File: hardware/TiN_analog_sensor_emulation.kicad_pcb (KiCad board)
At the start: 2 copper layers, 100 x 100 mm, 176 parts, among them J1 ADc, J2 Conn_01x04_Male, J3 Micro_SD_Card, J4 BOOT0, J5 Conn_01x03_Male, J6 display, J7 Barrel_Jack, J8 Conn_02x08_Odd_Even, SW2 SW_right, SW3 SW_middle2, SW4 SW_top, SW5 SW_middle, SW6 SW_bot, SW7 SW_Left, U1 STM32F042C6Tx, U10 MCP42010, U11 ADA4898-3, U12 ADA4898-3, U13 MCP42010, U14 MCP42010, U15 MCP42050, U16 MCP42050, U17 MCP42050, U18 LT1529CQ#PBF, U19 LT1528CQ, U2 ADA4898-3, U3 ADA4898-3, U4 MCP42010, U5 ADA4898-3, U6 ADA4898-3, U7 MCP42010, U8 ADA4898-3, U9 ADA4898-3, Y1 Crystal_GND24

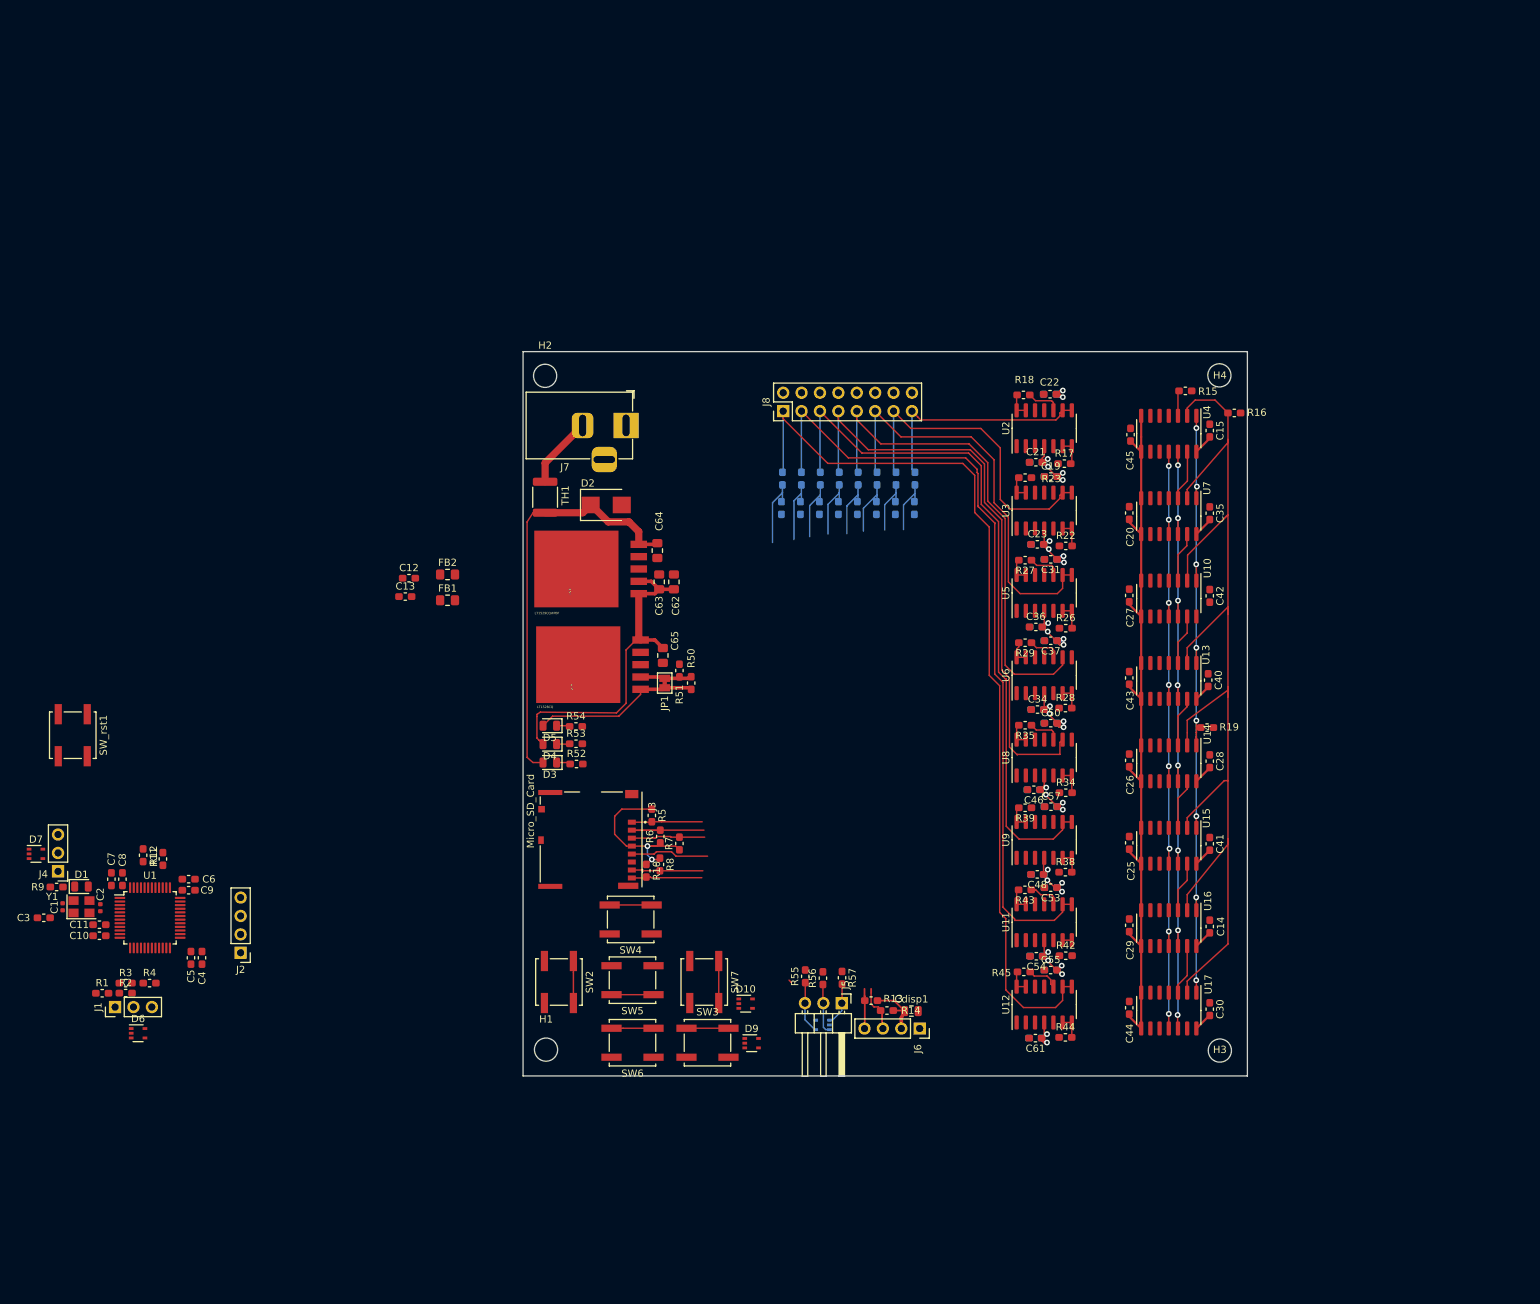
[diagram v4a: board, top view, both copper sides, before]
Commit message: layout gotów, do wyeliminowania błedy DRC
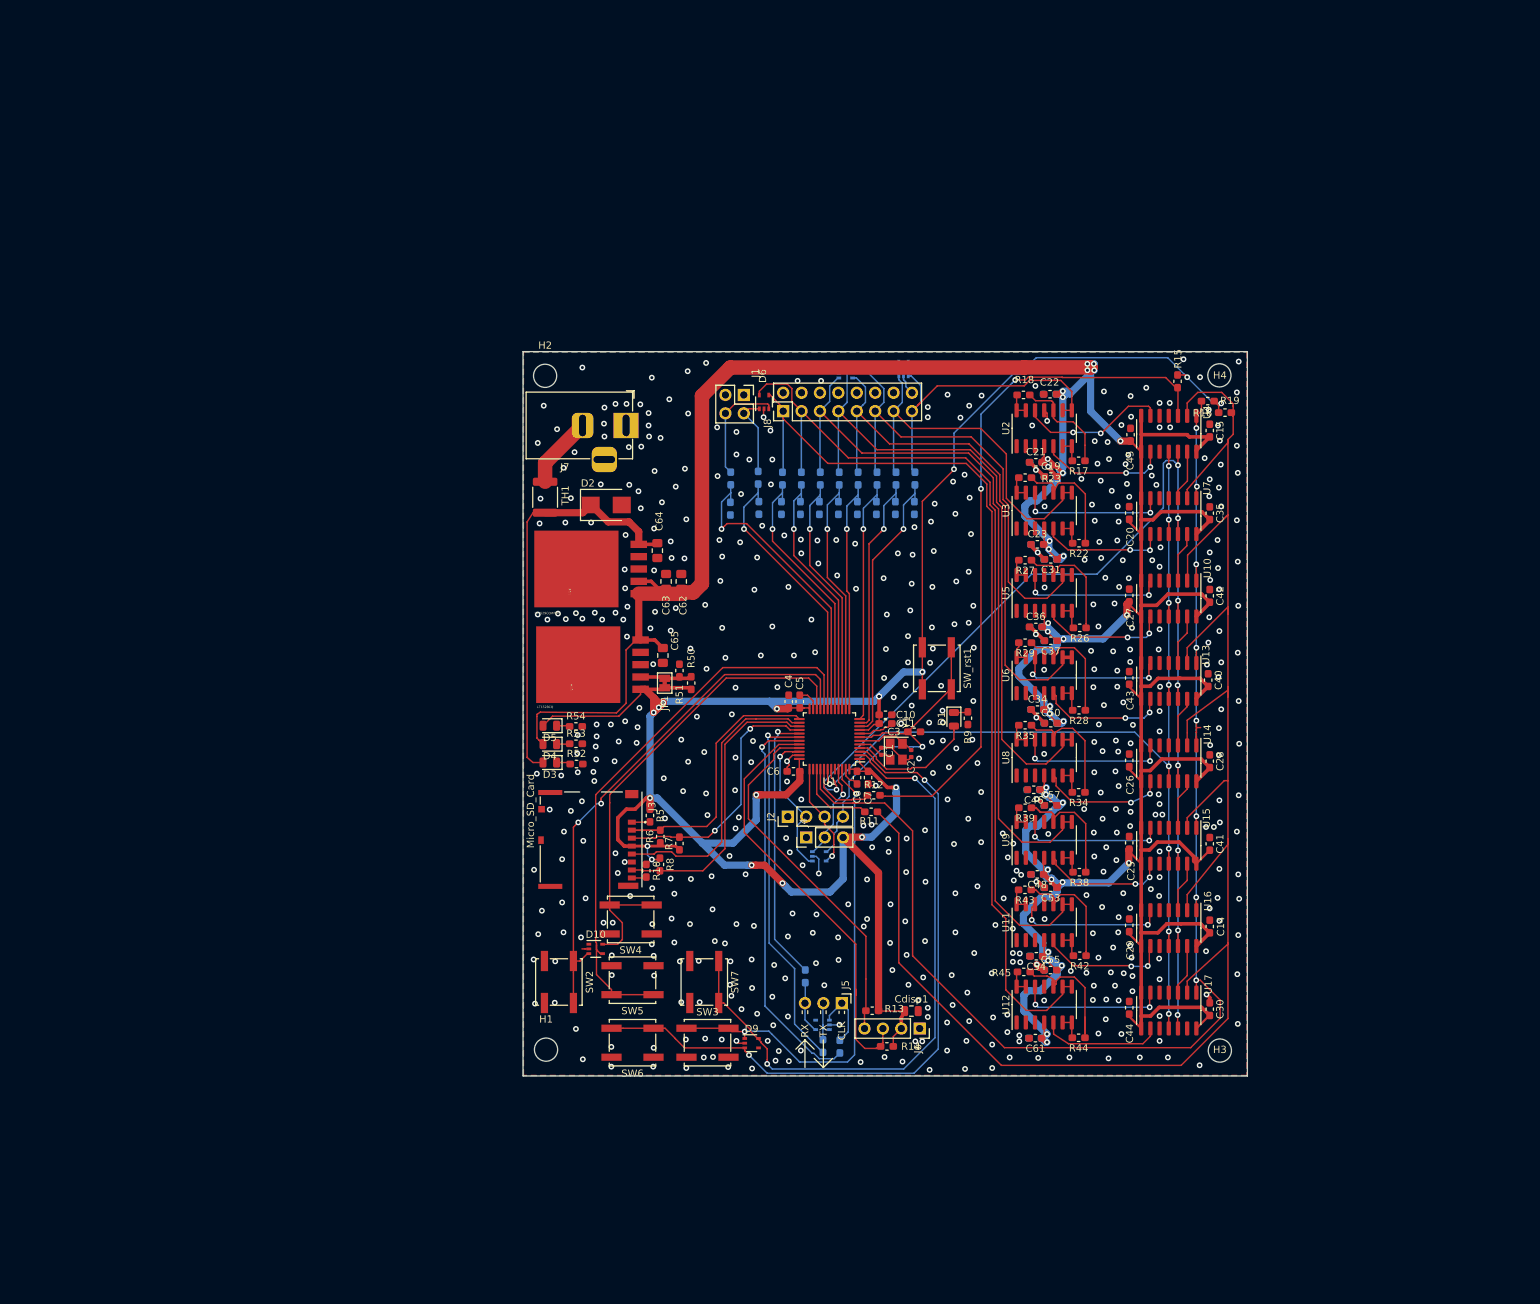
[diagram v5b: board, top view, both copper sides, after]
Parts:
- removed C12: 1u, Capacitor_SMD:C_0603_1608Metric_Pad1.05x0.95mm_HandSolder
- removed C13: 10n, Capacitor_SMD:C_0603_1608Metric_Pad1.05x0.95mm_HandSolder
- removed C9: 100n, Capacitor_SMD:C_0603_1608Metric_Pad1.05x0.95mm_HandSolder
- removed FB1, FB2: Ferrite_Bead_Small, Inductor_SMD:L_0805_2012Metric_Pad1.15x1.40mm_HandSolder
- added D11: PESD5V0L4UG, Package_TO_SOT_SMD:SOT-353_SC-70-5, B.Cu at (147.5, 52.4)
- added D12: PESD5V0L4UG, Package_TO_SOT_SMD:SOT-353_SC-70-5, B.Cu at (139.5, 53.0)
- D7, R1, R2, R3, R4, R55, R56, R57: moved to B.Cu
- J1: value ADc -> Conn_02x02_Odd_Even; footprint Connector_PinHeader_2.54mm:PinHeader_1x03_P2.54mm_Vertical -> Connector_PinHeader_2.54mm:PinHeader_2x02_P2.54mm_Vertical
- moved R9 127.9 mm to (156.4, 100.6), turned to 270 degrees
- moved C3 122.9 mm to (149.0, 102.5)
- moved D6 122.7 mm to (128.3, 56.9), turned to 90 degrees
- moved D1 122.6 mm to (154.5, 100.8), turned to 270 degrees
- moved J1 121.1 mm to (125.5, 56.0), turned to 270 degrees
- moved SW_rst1 119.6 mm to (152.1, 93.7)
- moved C1 115.0 mm to (144.4, 105.2), turned to 90 degrees
- moved Y1 114.5 mm to (146.5, 105.2), turned to 270 degrees
- moved C2 114.0 mm to (148.6, 105.5), turned to 90 degrees
- moved C10 112.7 mm to (145.0, 100.1), turned to 0 degrees
- moved R1 112.2 mm to (123.7, 67.5), turned to 270 degrees
- moved C11 112.0 mm to (145.0, 101.3), turned to 0 degrees
- moved R3 111.8 mm to (127.5, 67.4), turned to 270 degrees
- moved D7 108.1 mm to (135.9, 119.7)
- moved R2 107.0 mm to (123.6, 71.7), turned to 270 degrees
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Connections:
- C10 pad 2: GNDA -> GND
- C11 pad 2: GNDA -> GND
- C16 pad 2: GNDA -> GND
- C17 pad 1: GNDA -> GND
- C18 pad 2: GNDA -> GND
- C19 pad 1: GNDA -> GND
- C21 pad 1: GNDA -> GND
- C22 pad 2: GNDA -> GND
- C23 pad 1: GNDA -> GND
- C24 pad 2: GNDA -> GND
- C31 pad 2: GNDA -> GND
- C32 pad 1: GNDA -> GND
- C33 pad 2: GNDA -> GND
- C34 pad 1: GNDA -> GND
- C36 pad 1: GNDA -> GND
- C37 pad 2: GNDA -> GND
- C38 pad 1: GNDA -> GND
- C39 pad 2: GNDA -> GND
- C4 pad 2: +3V3 -> +3.3VA
- C46 pad 2: GNDA -> GND
- C47 pad 1: GNDA -> GND
- C48 pad 2: GNDA -> GND
- C49 pad 1: GNDA -> GND
- C5 pad 2: +3V3 -> +3.3VA
- C50 pad 1: GNDA -> GND
- C51 pad 2: GNDA -> GND
- C52 pad 1: GNDA -> GND
- C53 pad 2: GNDA -> GND
- C54 pad 2: GNDA -> GND
- C55 pad 1: GNDA -> GND
- C56 pad 2: GNDA -> GND
- C57 pad 1: GNDA -> GND
- C58 pad 1: GNDA -> GND
- C59 pad 2: GNDA -> GND
- C6 pad 1: +3V3 -> +3.3VA
- C60 pad 1: GNDA -> GND
- C61 pad 2: GNDA -> GND
- C7 pad 1: +3V3 -> +3.3VA
- C8 pad 2: +3V3 -> +3.3VA
- Cdisp1 pad 1: +3V3 -> +3.3VA
- D10 pad 1: (no net) -> Net-(D10-Pad1)
- D10 pad 3: (no net) -> /MCU/sw_left
- D10 pad 5: (no net) -> /MCU/sw_top
- D6 pad 4: (no net) -> /digital_pot/pot8
- D6 pad 5: (no net) -> /digital_pot/pot7
- D7 pad 5: (no net) -> /MCU/SWCLK
- D9 pad 1: /MCU/sw_right -> /MCU/sw_mid2
- D9 pad 4: /MCU/sw_left -> (no net)
- D9 pad 5: (no net) -> /MCU/sw_right
- J1 pad 1: Net-(D6-Pad1) -> GND
- J1 pad 2: Net-(D6-Pad3) -> Net-(D6-Pad1)
- J3 pad 4: +3V3 -> +3.3VA
- J4 pad 3: +3V3 -> +3.3VA
- J6 pad 2: +3V3 -> +3.3VA
- J8 pad 10: GNDA -> GND
- J8 pad 12: GNDA -> GND
- J8 pad 14: GNDA -> GND
- J8 pad 16: GNDA -> GND
- J8 pad 2: GNDA -> GND
- J8 pad 4: GNDA -> GND
- J8 pad 6: GNDA -> GND
- J8 pad 8: GNDA -> GND
- R10 pad 1: +3V3 -> +3.3VA
- R13 pad 1: +3V3 -> +3.3VA
- R14 pad 1: +3V3 -> +3.3VA
- R15 pad 1: +3V3 -> +3.3VA
- R16 pad 1: +3V3 -> +3.3VA
- R19 pad 1: +3V3 -> +3.3VA
- R5 pad 1: +3V3 -> +3.3VA
- R6 pad 1: +3V3 -> +3.3VA
- R7 pad 1: +3V3 -> +3.3VA
- R8 pad 1: +3V3 -> +3.3VA
- SW_rst1 pad 1: +3V3 -> +3.3VA
- U1 pad 1: +3V3 -> +3.3VA
- U1 pad 24: +3V3 -> +3.3VA
- U1 pad 36: +3V3 -> +3.3VA
- U1 pad 48: +3V3 -> +3.3VA
- U1 pad 8: GNDA -> GND
- U10 pad 10: GNDA -> GND
- U10 pad 5: GNDA -> GND
- U11 pad 1: GNDA -> GND
- U11 pad 11: GNDA -> GND
- U11 pad 2: GNDA -> GND
- U11 pad 3: GNDA -> GND
- U12 pad 1: GNDA -> GND
- U12 pad 11: GNDA -> GND
- U12 pad 2: GNDA -> GND
- U12 pad 3: GNDA -> GND
- U13 pad 10: GNDA -> GND
- U13 pad 5: GNDA -> GND
- U14 pad 10: GNDA -> GND
- U14 pad 5: GNDA -> GND
- U15 pad 10: GNDA -> GND
- U15 pad 5: GNDA -> GND
- U16 pad 10: GNDA -> GND
- U16 pad 5: GNDA -> GND
- U17 pad 10: GNDA -> GND
- U17 pad 5: GNDA -> GND
- U2 pad 1: GNDA -> GND
- U2 pad 11: GNDA -> GND
- U2 pad 2: GNDA -> GND
- U2 pad 3: GNDA -> GND
- U3 pad 1: GNDA -> GND
- U3 pad 11: GNDA -> GND
- U3 pad 2: GNDA -> GND
- U3 pad 3: GNDA -> GND
- U4 pad 10: GNDA -> GND
- U4 pad 5: GNDA -> GND
- U5 pad 1: GNDA -> GND
- U5 pad 11: GNDA -> GND
- U5 pad 2: GNDA -> GND
- U5 pad 3: GNDA -> GND
- U6 pad 1: GNDA -> GND
- U6 pad 11: GNDA -> GND
- U6 pad 2: GNDA -> GND
- U6 pad 3: GNDA -> GND
- U7 pad 10: GNDA -> GND
- U7 pad 5: GNDA -> GND
- U8 pad 1: GNDA -> GND
- U8 pad 11: GNDA -> GND
- U8 pad 2: GNDA -> GND
- U8 pad 3: GNDA -> GND
- U9 pad 1: GNDA -> GND
- U9 pad 11: GNDA -> GND
- U9 pad 2: GNDA -> GND
- U9 pad 3: GNDA -> GND
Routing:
- net +5V: track 264.1 -> 588.5 mm
- net +3.3VA: track 23.1 -> 325.5 mm, vias 0 -> 18
- net /digital_pot/CS: track 94.6 -> 188.8 mm
- net /MCU/sw_bot: track 5.80 -> 98.9 mm, vias 0 -> 2
- net /MCU/POTMOSI: track 3.50 -> 96.3 mm, vias 0 -> 2
- net /MCU/POTSCK: track 157.6 -> 247.8 mm
- net /MCU/sw_right: track 5.80 -> 88.7 mm, vias 0 -> 2
- net /MCU/POTSHDN: track 92.2 -> 169.0 mm, vias 8 -> 9
- net /MCU/sw_mid1: track 5.80 -> 79.9 mm
- net /MCU/sw_left: track 5.80 -> 74.4 mm, vias 0 -> 2
- net /MCU/sw_top: track 5.80 -> 68.5 mm
- net /MCU/sw_mid2: track 5.80 -> 67.2 mm, vias 0 -> 2
- net /MCU/USART_CK: track 0.00 -> 55.1 mm, vias 0 -> 1
- net /MCU/POTRST: track 91.7 -> 145.6 mm, vias 8 -> 9
- net /MCU/I2C_SCL: track 6.52 -> 59.5 mm
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- added copper zone on B.Cu, net GND
- added copper zone on F.Cu, net GND

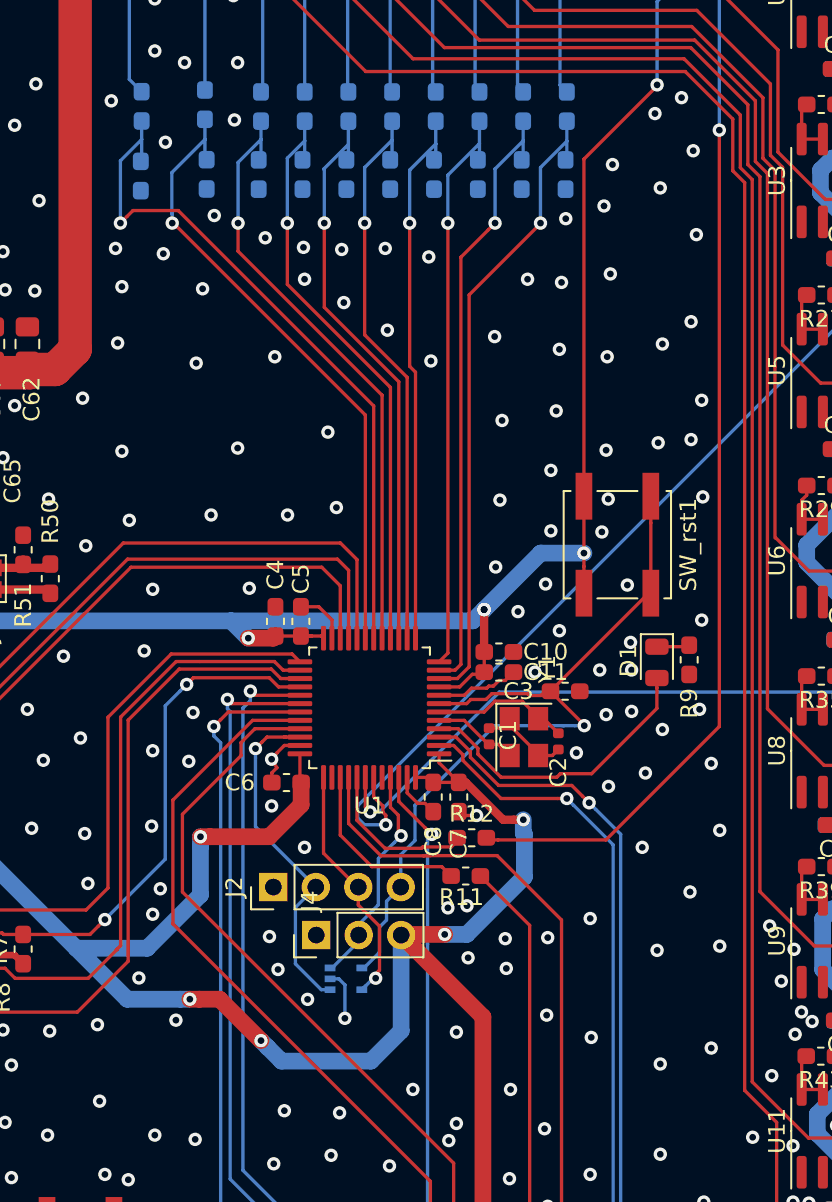
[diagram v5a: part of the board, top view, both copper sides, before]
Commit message: dodany otwór do montażu wyświetlacza
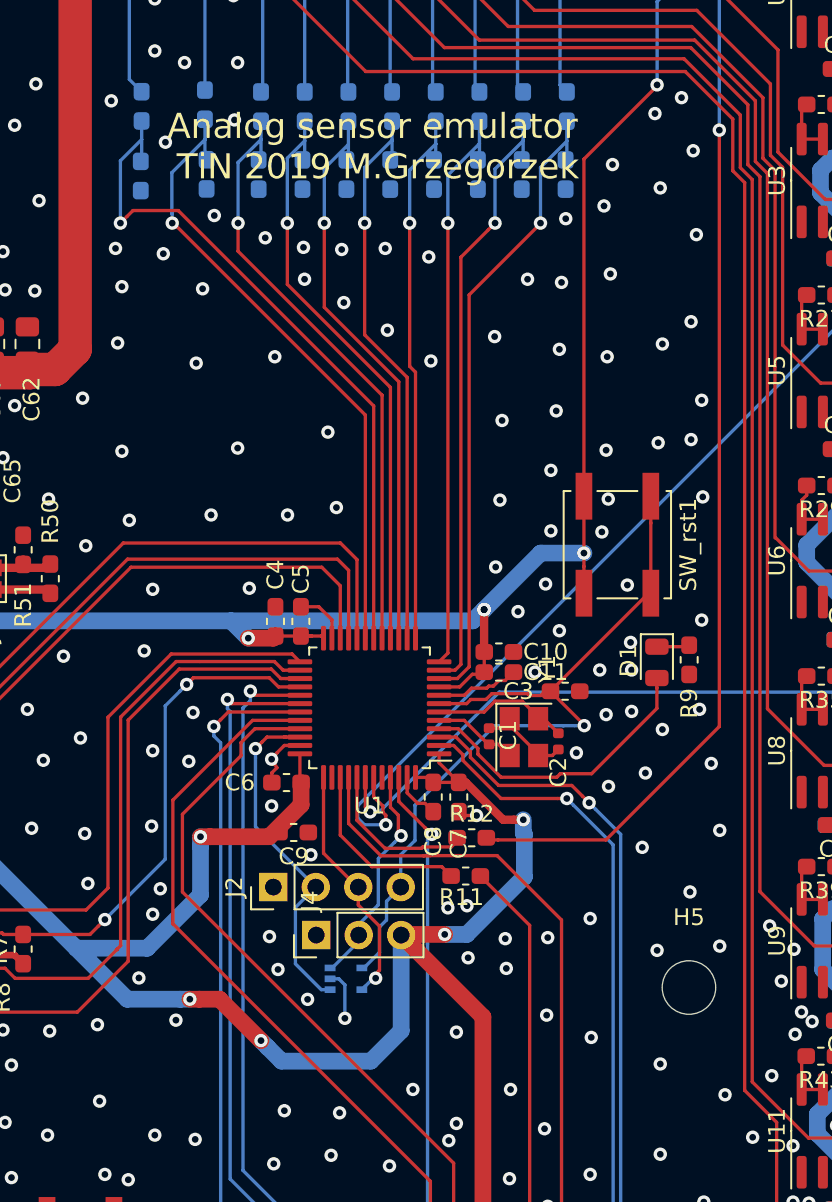
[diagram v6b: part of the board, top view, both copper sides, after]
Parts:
- added C9: 100n, Capacitor_SMD:C_0603_1608Metric_Pad1.05x0.95mm_HandSolder, F.Cu at (132.8, 110.9)
- added H5: MountingHole, MountingHole:MountingHole_3.2mm_M3, F.Cu at (156.4, 120.2)
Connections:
- D10 pad 1: Net-(D10-Pad1) -> (no net)
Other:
- board text added: "Analog sensor emulator TiN 2019 M.Grzegorzek"
